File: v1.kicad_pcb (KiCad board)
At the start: 2 copper layers, 60 parts, among them J1 Screw_Terminal_01x02, J2 Conn_02x08_Odd_Even, J3 Conn_01x03_Male, J4 Screw_Terminal_01x04, U1 LT3959, U2 LT3959, U3 LT3959

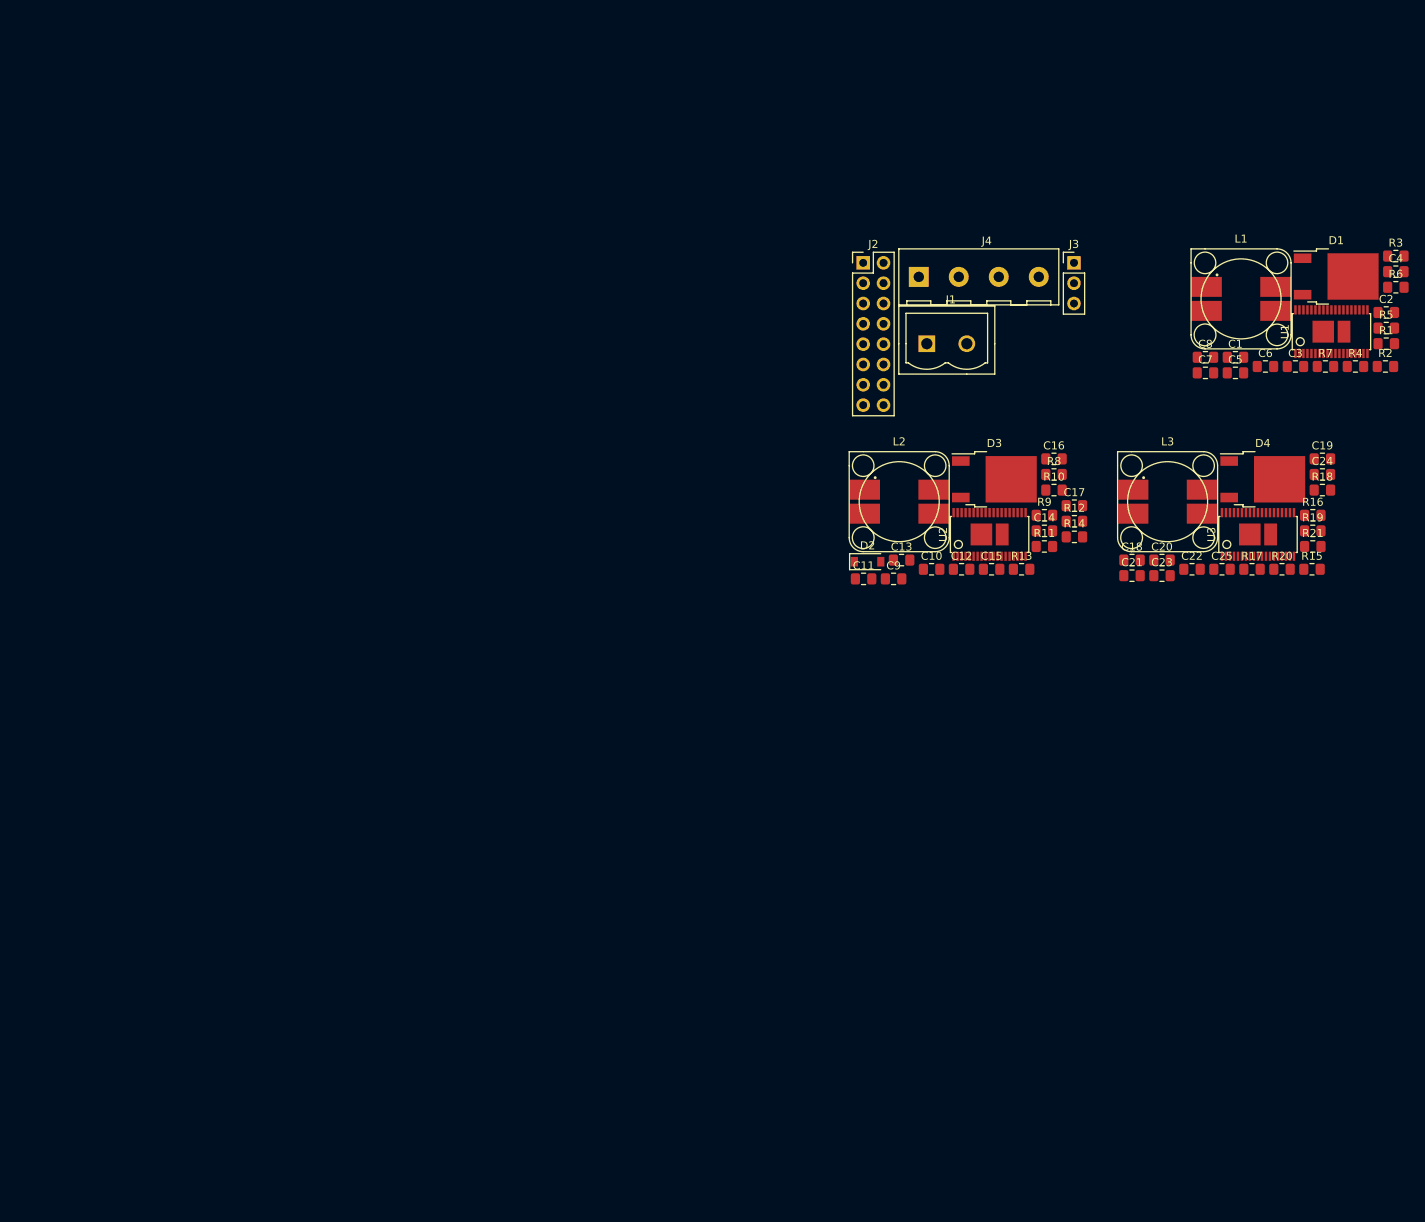
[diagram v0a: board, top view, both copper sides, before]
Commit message: Started laying out
shared inductor is a pain, so we're splitting into 2
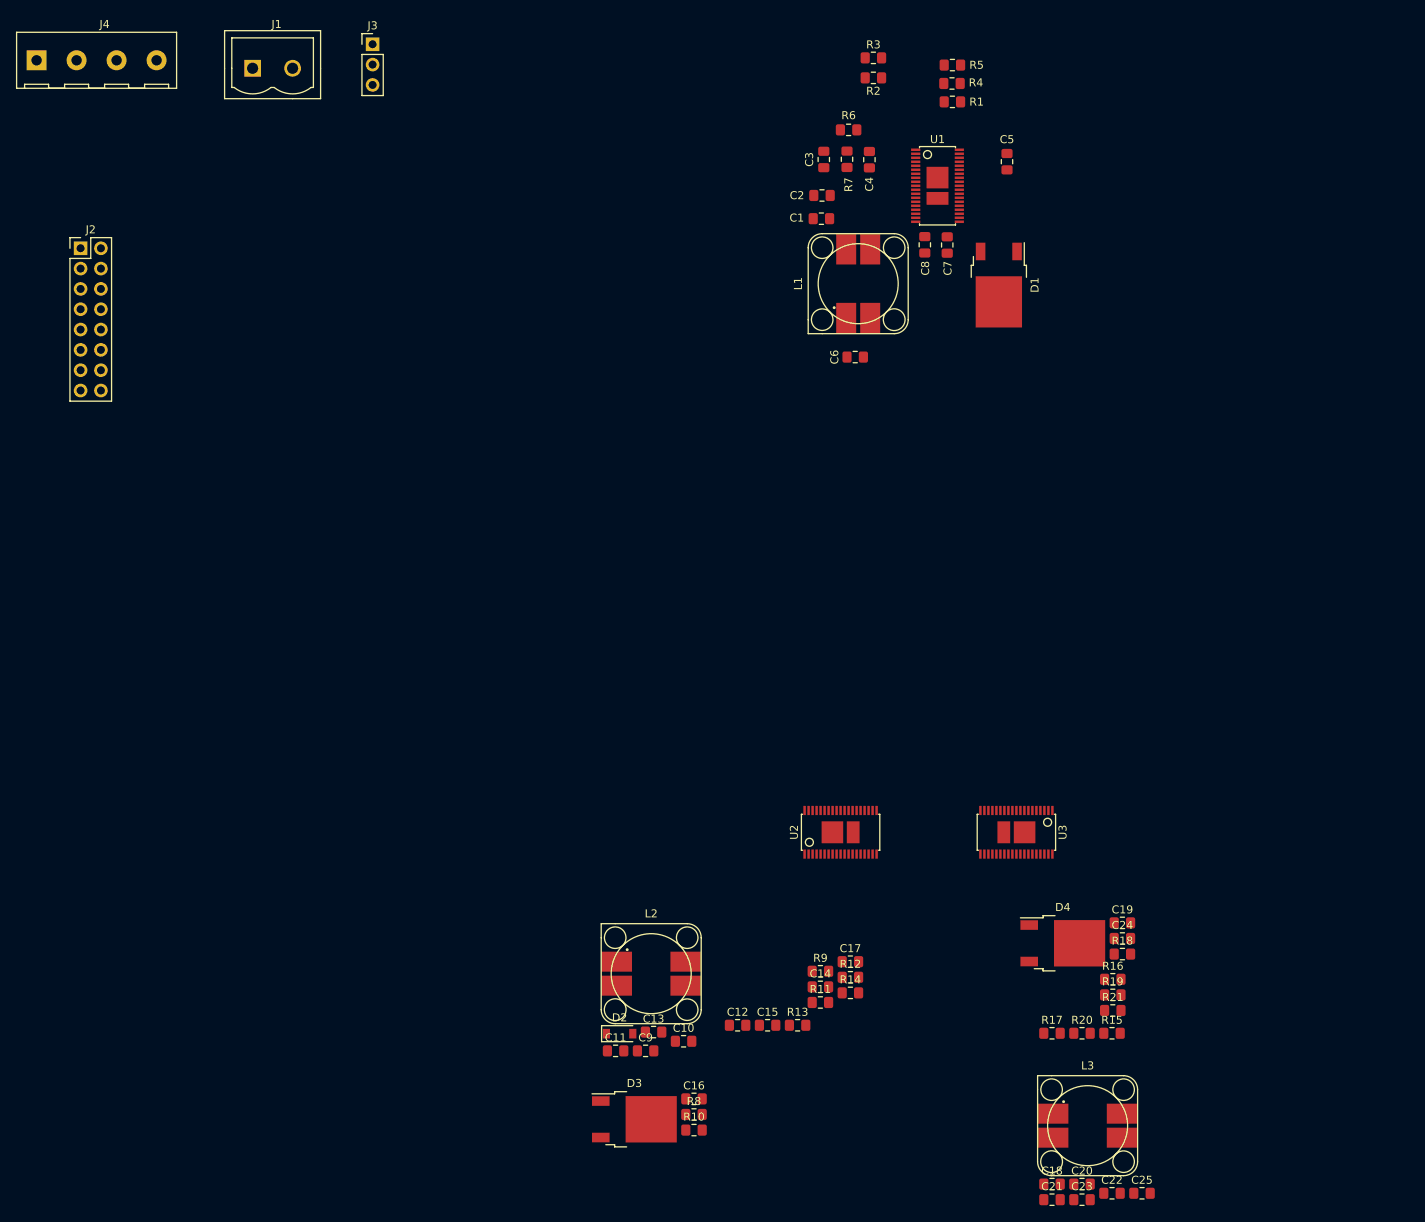
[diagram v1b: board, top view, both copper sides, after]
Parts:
- moved J4 113.6 mm to (18.5, 38.5)
- moved J2 97.8 mm to (24.0, 62.0)
- moved J3 91.8 mm to (60.5, 36.5)
- moved C16 91.8 mm to (100.7, 168.3)
- moved D3 91.8 mm to (93.2, 170.9)
- moved R10 91.8 mm to (100.7, 172.2)
- moved R8 91.8 mm to (100.7, 170.3)
- moved J1 91.0 mm to (45.5, 39.5)
- moved C21 78.6 mm to (145.4, 180.9)
- moved C23 78.6 mm to (149.2, 180.9)
- moved L3 78.6 mm to (149.9, 171.7)
- moved C22 78.6 mm to (152.9, 180.1)
- moved C25 78.6 mm to (156.7, 180.1)
- moved C18 78.6 mm to (145.4, 179.0)
- moved C20 78.6 mm to (149.2, 179.0)
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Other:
- copper layers 2 -> 4
- net class sw added: clearance 0.2, trace_width 7, via_dia 0.8, via_drill 0.4

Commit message: Named nets, made it use 2 inductors
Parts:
- added L4: SRP1265A-330M, bourns:bourns_srp1265a, F.Cu at (155.1, 46.9)
- added L5: SRP1265A-330M, bourns:bourns_srp1265a, F.Cu at (161.8, 133.0)
- added L6: SRP1265A-330M, bourns:bourns_srp1265a, F.Cu at (116.9, 168.8)
- L1, L2, L3: value DRQ127-150 -> SRP1265A-330M; footprint eaton:eaton_drq127 -> bourns:bourns_srp1265a
- moved C6 12.4 mm to (131.9, 70.1)
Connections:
- net Net-(C13-Pad2) renamed /negative 12V supply/INTVCC
- net Net-(C14-Pad1) renamed /negative 12V supply/DRIVE
- net Net-(R10-Pad1) renamed /negative 12V supply/EN_UVLO
- net Net-(R13-Pad2) renamed /negative 12V supply/FBX
- net Net-(R16-Pad2) renamed /positive5Vsupply/FBX
- net Net-(R18-Pad2) renamed /positive5Vsupply/EN_UVLO
- net Net-(R2-Pad2) renamed /positive 12V supply/FBX
- net Net-(R4-Pad2) renamed /positive 12V supply/EN_UVLO
- C11 pad 2: Net-(C11-Pad2) -> /negative 12V supply/SGND
- C12 pad 2: Net-(C11-Pad2) -> /negative 12V supply/SGND
- C13 pad 1: Net-(C11-Pad2) -> /negative 12V supply/SGND
- C15 pad 1: Net-(C15-Pad1) -> /negative 12V supply/DRIVE_DIODE_IN
- C15 pad 2: Net-(C15-Pad2) -> /negative 12V supply/GND_DIODE_IN
- C20 pad 2: Net-(C20-Pad2) -> /positive5Vsupply/SGND
- C21 pad 2: Net-(C20-Pad2) -> /positive5Vsupply/SGND
- C22 pad 1: Net-(C20-Pad2) -> /positive5Vsupply/SGND
- C23 pad 1: Net-(C23-Pad1) -> /positive5Vsupply/SW
- C23 pad 2: Net-(C23-Pad2) -> /positive5Vsupply/DIODE_IN
- C24 pad 1: +5Vcc -> +12Vcc
- C25 pad 1: +5Vcc -> +12Vcc
- C3 pad 2: Net-(C3-Pad2) -> /positive 12V supply/SGND
- C4 pad 2: Net-(C3-Pad2) -> /positive 12V supply/SGND
- C5 pad 1: Net-(C3-Pad2) -> /positive 12V supply/SGND
- C6 pad 1: Net-(C6-Pad1) -> /positive 12V supply/SW
- C6 pad 2: Net-(C6-Pad2) -> /positive 12V supply/DIODE_IN
- D1 pad 2: Net-(C6-Pad2) -> /positive 12V supply/DIODE_IN
- D2 pad 2: Net-(C15-Pad1) -> /negative 12V supply/DRIVE_DIODE_IN
- D3 pad 2: Net-(C15-Pad2) -> /negative 12V supply/GND_DIODE_IN
- D4 pad 1: +5Vcc -> +12Vcc
- D4 pad 2: Net-(C23-Pad2) -> /positive5Vsupply/DIODE_IN
- L1 pad 1: Net-(C6-Pad1) -> Vin2.5-24V
- L1 pad 2: Net-(C6-Pad2) -> /positive 12V supply/SW
- L2 pad 2: -12Vcc -> /negative 12V supply/DRIVE_DIODE_IN
- L3 pad 1: Net-(C23-Pad1) -> Vin2.5-24V
- L3 pad 2: Net-(C23-Pad2) -> /positive5Vsupply/SW
- R10 pad 2: Net-(C11-Pad2) -> /negative 12V supply/SGND
- R12 pad 2: Net-(C11-Pad2) -> /negative 12V supply/SGND
- R14 pad 2: Net-(C11-Pad2) -> /negative 12V supply/SGND
- R16 pad 1: +5Vcc -> +12Vcc
- R17 pad 2: Net-(C20-Pad2) -> /positive5Vsupply/SGND
- R19 pad 2: Net-(C20-Pad2) -> /positive5Vsupply/SGND
- R21 pad 2: Net-(C20-Pad2) -> /positive5Vsupply/SGND
- R3 pad 2: Net-(C3-Pad2) -> /positive 12V supply/SGND
- R5 pad 2: Net-(C3-Pad2) -> /positive 12V supply/SGND
- R7 pad 2: Net-(C3-Pad2) -> /positive 12V supply/SGND
- U1 pad 1: (no net) -> Earth
- U1 pad 10: Net-(C3-Pad2) -> /positive 12V supply/SGND
- U1 pad 11: (no net) -> /positive 12V supply/SGND
- U1 pad 12: Net-(C6-Pad1) -> /positive 12V supply/SW
- U1 pad 13: (no net) -> /positive 12V supply/SW
- U1 pad 14: (no net) -> /positive 12V supply/SW
- U1 pad 15: Net-(C6-Pad1) -> /positive 12V supply/SW
- U1 pad 16: (no net) -> /positive 12V supply/SW
- U1 pad 17: Net-(C3-Pad2) -> /positive 12V supply/SGND
- U1 pad 2: (no net) -> Earth
- U1 pad 23: Net-(U1-Pad23) -> /positive 12V supply/SW
- U1 pad 24: Net-(C6-Pad1) -> /positive 12V supply/SW
- U1 pad 25: Net-(U1-Pad25) -> /positive 12V supply/SW
- U1 pad 26: Net-(U1-Pad26) -> /positive 12V supply/SW
- U1 pad 27: Net-(C6-Pad1) -> /positive 12V supply/SW
- U1 pad 28: Net-(U1-Pad28) -> /positive 12V supply/SGND
- U1 pad 29: Net-(C3-Pad2) -> /positive 12V supply/SGND
- U1 pad 3: (no net) -> Earth
- U1 pad 35: (no net) -> Earth
- U1 pad 36: (no net) -> Earth
- U1 pad 37: (no net) -> Earth
- U1 pad 38: (no net) -> Earth
- U1 pad 8: Net-(C3-Pad2) -> /positive 12V supply/SGND
- U2 pad 1: (no net) -> Earth
- U2 pad 10: Net-(C11-Pad2) -> /negative 12V supply/SGND
- U2 pad 11: (no net) -> /negative 12V supply/SGND
- U2 pad 12: Net-(C15-Pad1) -> /negative 12V supply/DRIVE_DIODE_IN
- U2 pad 13: (no net) -> /negative 12V supply/DRIVE_DIODE_IN
- U2 pad 14: (no net) -> /negative 12V supply/DRIVE_DIODE_IN
- U2 pad 15: Net-(C15-Pad1) -> /negative 12V supply/DRIVE_DIODE_IN
- U2 pad 16: (no net) -> /negative 12V supply/DRIVE_DIODE_IN
- U2 pad 17: Net-(C11-Pad2) -> /negative 12V supply/SGND
- U2 pad 2: (no net) -> Earth
- U2 pad 23: Net-(U2-Pad23) -> /negative 12V supply/DRIVE_DIODE_IN
- U2 pad 24: Net-(C15-Pad1) -> /negative 12V supply/DRIVE_DIODE_IN
- U2 pad 25: Net-(U2-Pad25) -> /negative 12V supply/DRIVE_DIODE_IN
- U2 pad 26: Net-(U2-Pad26) -> /negative 12V supply/DRIVE_DIODE_IN
- U2 pad 27: Net-(C15-Pad1) -> /negative 12V supply/DRIVE_DIODE_IN
- U2 pad 28: Net-(U2-Pad28) -> /negative 12V supply/SGND
- U2 pad 29: Net-(C11-Pad2) -> /negative 12V supply/SGND
- U2 pad 3: (no net) -> Earth
- U2 pad 30: Net-(U2-Pad30) -> /negative 12V supply/SGND
- U2 pad 35: (no net) -> Earth
- U2 pad 36: (no net) -> Earth
- U2 pad 37: (no net) -> Earth
- U2 pad 38: (no net) -> Earth
- U2 pad 8: Net-(C11-Pad2) -> /negative 12V supply/SGND
- U3 pad 1: (no net) -> Earth
- U3 pad 10: Net-(C20-Pad2) -> /positive5Vsupply/SGND
- U3 pad 11: (no net) -> /positive5Vsupply/SGND
- U3 pad 12: Net-(C23-Pad1) -> /positive5Vsupply/SW
- U3 pad 13: (no net) -> /positive5Vsupply/SW
- U3 pad 14: (no net) -> /positive5Vsupply/SW
- U3 pad 15: Net-(C23-Pad1) -> /positive5Vsupply/SW
- U3 pad 16: (no net) -> /positive5Vsupply/SW
- U3 pad 17: Net-(C20-Pad2) -> /positive5Vsupply/SGND
- U3 pad 2: (no net) -> Earth
- U3 pad 23: Net-(U3-Pad23) -> /positive5Vsupply/SW
- U3 pad 24: Net-(C23-Pad1) -> /positive5Vsupply/SW
- U3 pad 25: Net-(U3-Pad25) -> /positive5Vsupply/SW
- U3 pad 26: Net-(U3-Pad26) -> /positive5Vsupply/SW
- U3 pad 27: Net-(C23-Pad1) -> /positive5Vsupply/SW
- U3 pad 28: Net-(U3-Pad28) -> /positive5Vsupply/SGND
- U3 pad 29: Net-(C20-Pad2) -> /positive5Vsupply/SGND
- U3 pad 3: (no net) -> Earth
- U3 pad 32: +5Vcc -> +12Vcc
- U3 pad 35: (no net) -> Earth
- U3 pad 36: (no net) -> Earth
- U3 pad 37: (no net) -> Earth
- U3 pad 38: (no net) -> Earth
- U3 pad 8: Net-(C20-Pad2) -> /positive5Vsupply/SGND

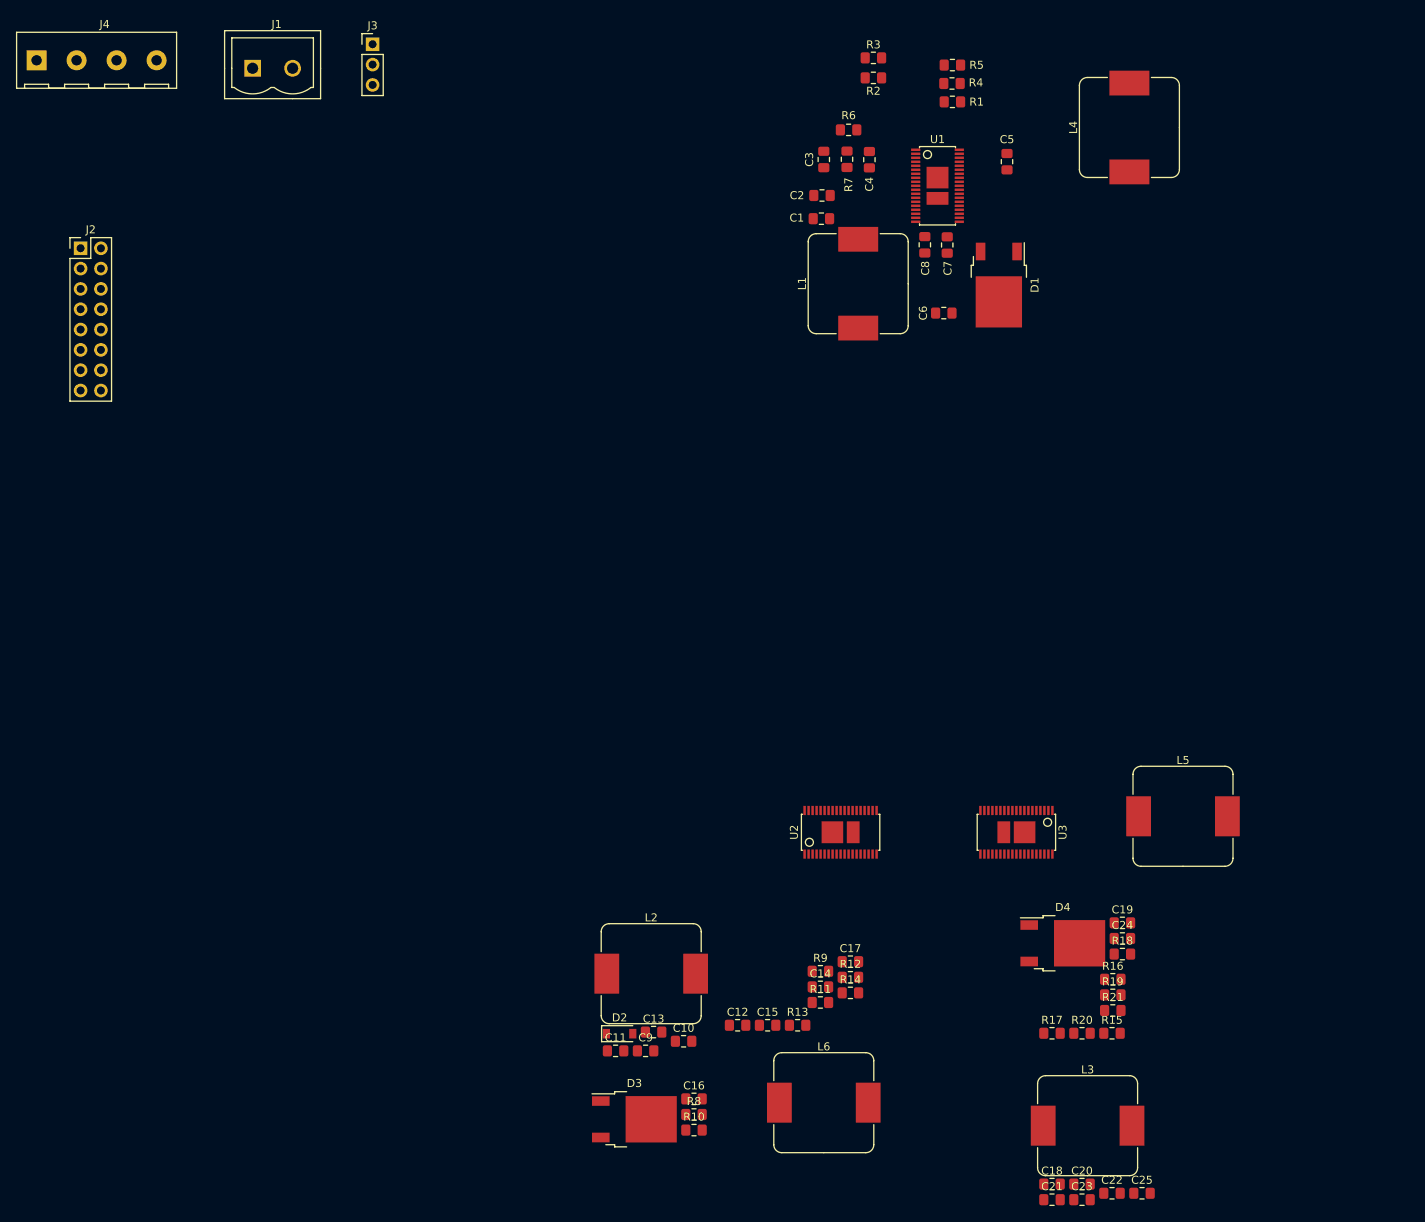
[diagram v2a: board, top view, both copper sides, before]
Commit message: Layed out inductors,
Now just have to lay out resistors that configure the power supply
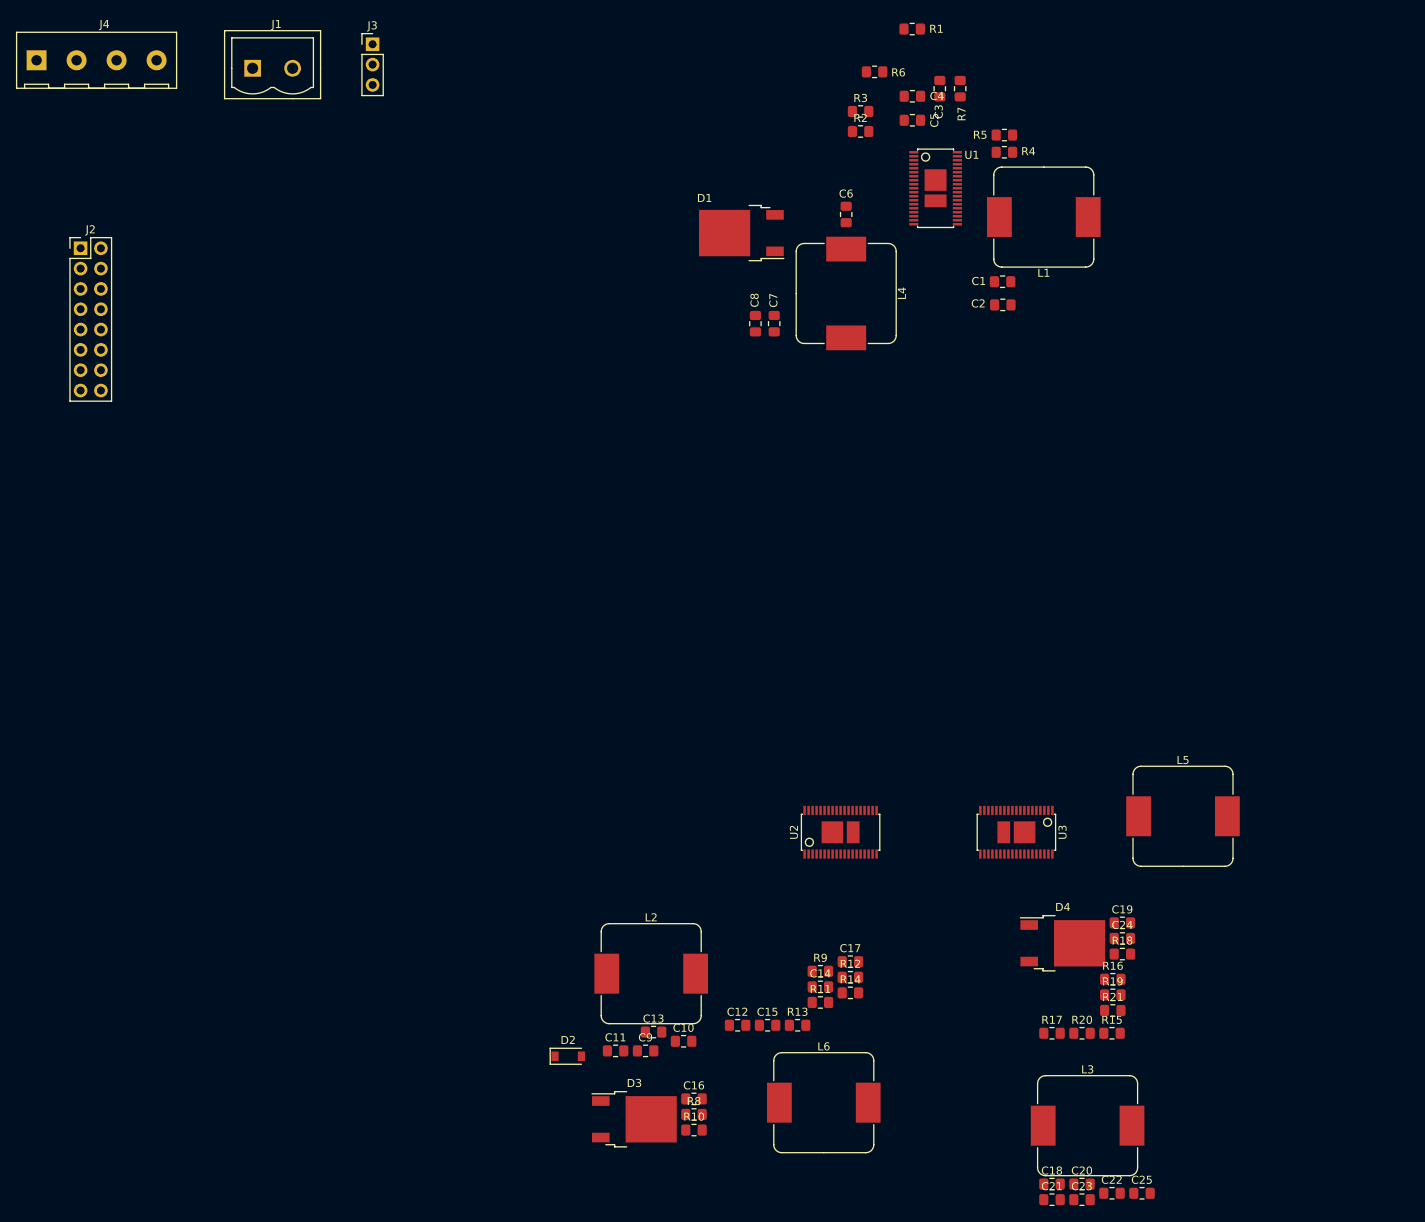
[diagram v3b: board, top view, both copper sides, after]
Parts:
- D1, D3, D4: footprint Package_TO_SOT_SMD:TO-252-2 -> generic:D_TO-252
- moved L4 41.0 mm to (119.7, 67.7), turned to 270 degrees
- moved D1 32.8 mm to (106.6, 60.1), turned to 180 degrees
- moved C2 26.4 mm to (139.3, 69.1), turned to 180 degrees
- moved L1 24.6 mm to (144.4, 58.1), turned to 180 degrees
- moved C1 24.0 mm to (139.3, 66.2), turned to 180 degrees
- moved C7 23.8 mm to (110.7, 71.4), turned to 270 degrees
- moved C8 23.4 mm to (108.3, 71.4), turned to 270 degrees
- moved C6 17.3 mm to (119.7, 57.8), turned to 270 degrees
- moved C3 17.0 mm to (131.4, 42.0)
- moved R7 16.7 mm to (133.9, 42.0)
- moved C5 12.9 mm to (128.0, 46.0), turned to 180 degrees
- moved R5 10.9 mm to (139.5, 47.9), turned to 180 degrees
- moved R4 10.8 mm to (139.5, 50.0)
- moved R1 10.4 mm to (128.0, 34.6)
- moved C4 9.58 mm to (128.0, 43.0), turned to 0 degrees
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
